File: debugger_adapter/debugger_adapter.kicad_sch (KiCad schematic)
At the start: 13 parts, among them X1 FT_CONN0_TAG, X10 FT_CONN_BREAKOUT, X11 DUT_CONN0_BREAKOUT, X12 VCC_SEL_UART, X13 DUT_CONN1_BREAKOUT, X2 FT_CONN1_TAG, X3 TAG_CONN_TAG, X4 FT_CONN_JTAG, X5 DUT_CONN_JTAG, X6 VCC_SEL_TAG, X7 VCC_SEL_JTAG, X8 FT_CONN_UART, X9 DUT_CONN_UART

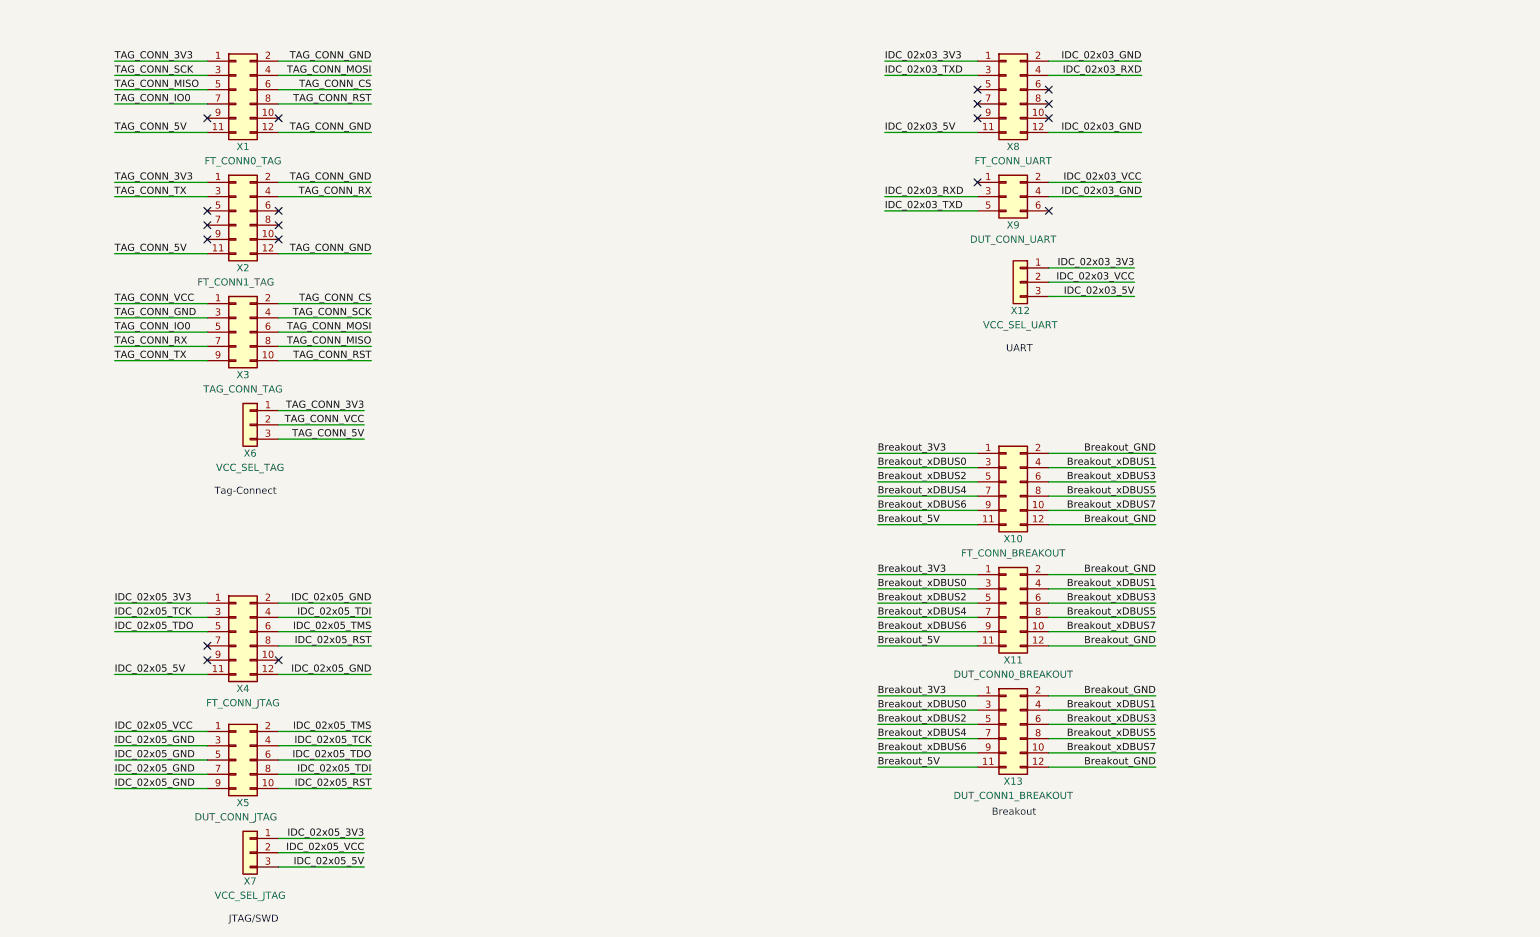
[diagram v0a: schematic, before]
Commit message: decrease clearance of copper pours
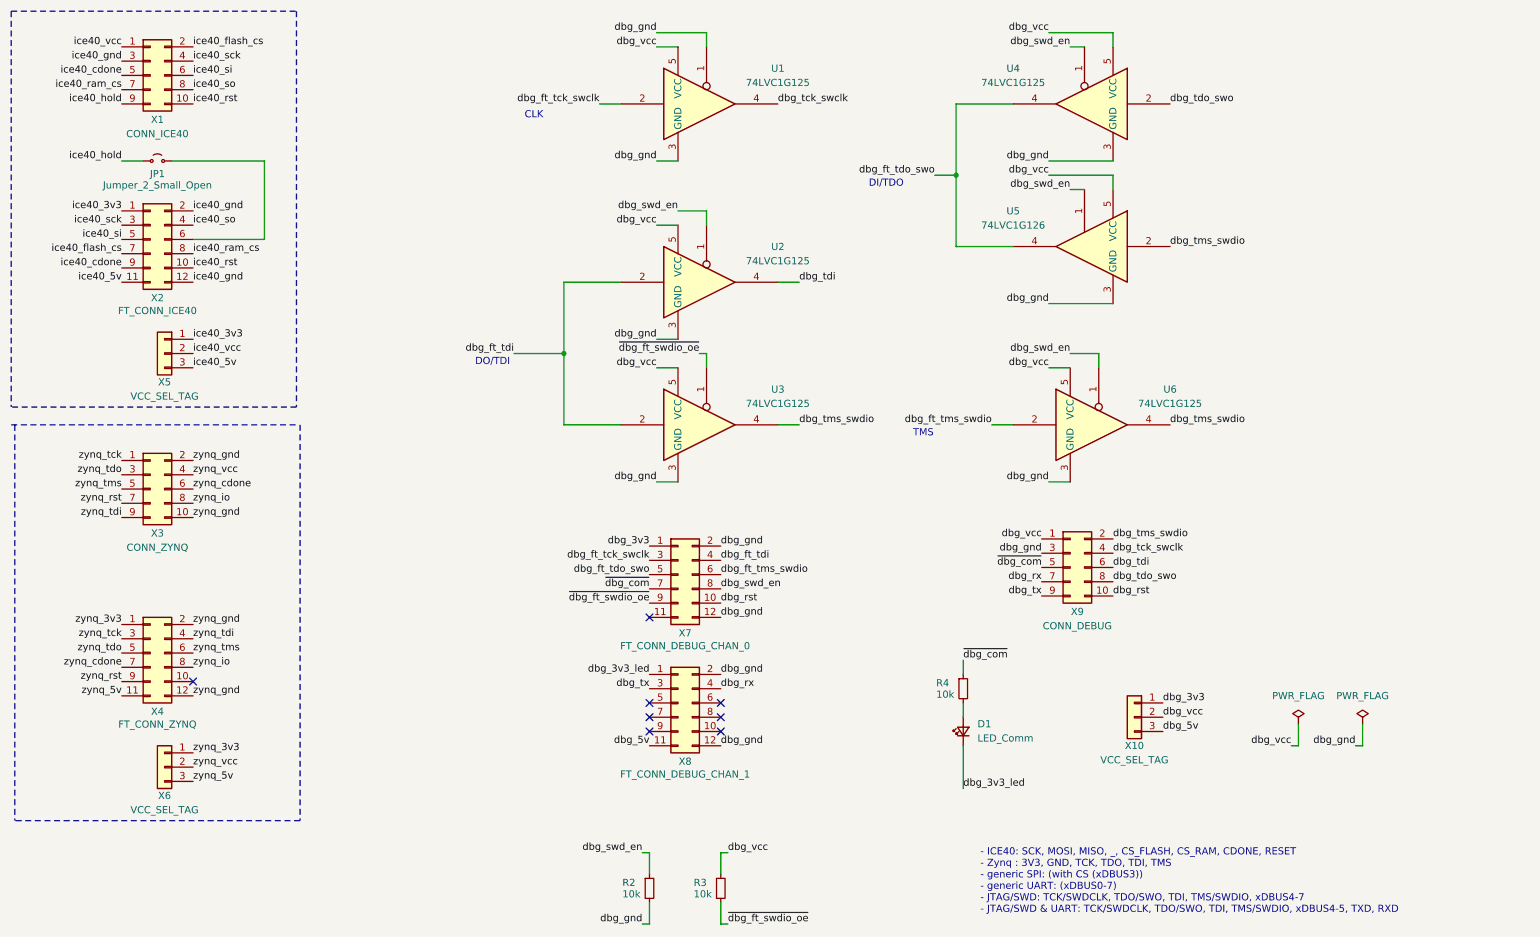
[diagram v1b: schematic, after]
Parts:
- removed X1: FT_CONN0_TAG, ft4232_debugger:header_male_02x06_HDRRA12W67P254_2X6_1524X254X503P, symbol Connector_Generic:Conn_02x06_Odd_Even
- removed X10: FT_CONN_BREAKOUT, ft4232_debugger:header_male_02x06_HDRRA12W67P254_2X6_1524X254X503P, symbol Connector_Generic:Conn_02x06_Odd_Even
- removed X11: DUT_CONN0_BREAKOUT, Connector_PinHeader_2.54mm:PinHeader_2x06_P2.54mm_Vertical_SMD, symbol Connector_Generic:Conn_02x06_Odd_Even
- removed X12: VCC_SEL_UART, Connector_PinHeader_2.54mm:PinHeader_1x03_P2.54mm_Vertical, symbol Connector_Generic:Conn_01x03
- removed X13: DUT_CONN1_BREAKOUT, Connector_PinHeader_2.54mm:PinHeader_2x06_P2.54mm_Vertical_SMD, symbol Connector_Generic:Conn_02x06_Odd_Even
- removed X5: DUT_CONN_JTAG, Connector_PinHeader_2.54mm:PinHeader_2x05_P2.54mm_Vertical_SMD, symbol Connector_Generic:Conn_02x05_Odd_Even
- removed X7: VCC_SEL_JTAG, Connector_PinHeader_2.54mm:PinHeader_1x03_P2.54mm_Vertical, symbol Connector_Generic:Conn_01x03
- removed X9: DUT_CONN_UART, ft4232_debugger:header_male_02x06_HDRRA12W67P254_2X6_1524X254X503P, symbol Connector_Generic:Conn_02x03_Odd_Even
- added D1: LED_Comm, LED_SMD:LED_0603_1608Metric, symbol Device:LED_Small
- added JP1: Jumper_2_Small_Open, Connector_PinHeader_2.54mm:PinHeader_1x02_P2.54mm_Vertical, symbol Jumper:Jumper_2_Small_Open
- added R2, R3, R4: 10k, Resistor_SMD:R_0402_1005Metric, symbol Device:R_Small
- added U1, U2, U3, U4, U6: 74LVC1G125, Package_TO_SOT_SMD:SOT-353_SC-70-5, symbol 74xGxx:74LVC1G125
- added U5: 74LVC1G126, Package_TO_SOT_SMD:SOT-353_SC-70-5, symbol 74xGxx:74LVC1G126
- added X1: CONN_ICE40, Connector_IDC:IDC-Header_2x05_P2.54mm_Vertical, symbol Connector_Generic:Conn_02x05_Odd_Even
- added X10, X5: VCC_SEL_TAG, Connector_PinHeader_2.54mm:PinHeader_1x03_P2.54mm_Vertical, symbol Connector_Generic:Conn_01x03
- added X7: FT_CONN_DEBUG_CHAN_0, ft4232_debugger:header_male_02x06_HDRRA12W67P254_2X6_1524X254X503P, symbol Connector_Generic:Conn_02x06_Odd_Even
- added X9: CONN_DEBUG, Connector_IDC:IDC-Header_2x05_P2.54mm_Vertical, symbol Connector_Generic:Conn_02x05_Odd_Even
- X2: value FT_CONN1_TAG -> FT_CONN_ICE40
- X3: value TAG_CONN_TAG -> CONN_ZYNQ; footprint Connector_PinHeader_2.54mm:PinHeader_2x05_P2.54mm_Vertical_SMD -> Connector_IDC:IDC-Header_2x05_P2.54mm_Vertical
- X4: value FT_CONN_JTAG -> FT_CONN_ZYNQ
- X8: value FT_CONN_UART -> FT_CONN_DEBUG_CHAN_1
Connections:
- net TAG_CONN_CS is gone; now on net zynq_gnd: X3.2 (Pin_2)
- net TAG_CONN_IO0 is gone; now on net zynq_tms: X3.5 (Pin_5)
- net TAG_CONN_MISO is gone; now on net zynq_io: X3.8 (Pin_8)
- net TAG_CONN_MOSI is gone; now on net zynq_cdone: X3.6 (Pin_6)
- net TAG_CONN_RST is gone; now on net zynq_gnd: X3.10 (Pin_10)
- net zynq_cdone: now reaches X4.7 (Pin_7)
- net zynq_rst: now reaches X4.9 (Pin_9)
- net zynq_rst: now also X3.7 (Pin_7)
- net ice40_rst: now reaches X2.10 (Pin_10)
- net ice40_rst: now also X1.10 (Pin_10)
- net ice40_si: now reaches X2.5 (Pin_5)
- net ice40_si: now also X1.6 (Pin_6)
- net at X2.6 (Pin_6): now also JP1.2 (B)
- net ice40_flash_cs: now reaches X2.7 (Pin_7)
- net ice40_flash_cs: now also X1.2 (Pin_2)
- net ice40_ram_cs: now reaches X2.8 (Pin_8)
- net ice40_ram_cs: now also X1.7 (Pin_7)
- net ice40_cdone: now reaches X2.9 (Pin_9)
- net ice40_cdone: now also X1.5 (Pin_5)
- net IDC_02x03_3V3 renamed dbg_3v3_led
- net dbg_3v3_led: now also D1.1 (K)
- net IDC_02x03_5V renamed dbg_5v
- net dbg_5v: now also X10.3 (Pin_3)
- net IDC_02x03_GND renamed dbg_gnd
- net dbg_gnd: now also R2.2, U1.1, U1.3 (GND), U2.3 (GND), U3.3 (GND), U4.3 (GND), U5.3 (GND), U6.3 (GND), X7.12 (Pin_12), X7.2 (Pin_2), X9.3 (Pin_3)
- net IDC_02x03_RXD renamed dbg_rx
- net dbg_rx: now also X9.7 (Pin_7)
- net IDC_02x03_TXD renamed dbg_tx
- net dbg_tx: now also X9.9 (Pin_9)
- net IDC_02x05_3V3 renamed zynq_3v3
- net zynq_3v3: now also X6.1 (Pin_1)
- net IDC_02x05_5V renamed zynq_5v
- net zynq_5v: now also X6.3 (Pin_3)
- net IDC_02x05_GND renamed zynq_gnd
- net IDC_02x05_RST renamed zynq_io
- net IDC_02x05_TCK renamed zynq_tck
- net zynq_tck: now also X3.1 (Pin_1)
- net IDC_02x05_TDI renamed zynq_tdi
- net zynq_tdi: now also X3.9 (Pin_9)
- net IDC_02x05_TDO renamed zynq_tdo
- net zynq_tdo: now also X3.3 (Pin_3)
- net IDC_02x05_TMS renamed zynq_tms
- net TAG_CONN_3V3 renamed ice40_3v3
- net ice40_3v3: now also X5.1 (Pin_1); no longer X6.1 (Pin_1)
- net TAG_CONN_5V renamed ice40_5v
- net ice40_5v: now also X5.3 (Pin_3); no longer X6.3 (Pin_3)
- net TAG_CONN_GND renamed ice40_gnd
- net ice40_gnd: now also X1.3 (Pin_3); no longer X3.3 (Pin_3)
- net TAG_CONN_RX renamed ice40_so
- net ice40_so: now also X1.8 (Pin_8); no longer X3.7 (Pin_7)
- net TAG_CONN_SCK renamed zynq_vcc
- net zynq_vcc: now also X6.2 (Pin_2)
- net TAG_CONN_TX renamed ice40_sck
- net ice40_sck: now also X1.4 (Pin_4); no longer X3.9 (Pin_9)
- removed net TAG_CONN_VCC: X3.1 (Pin_1), X6.2 (Pin_2)
- new net: D1.2 (A), R4.2
- new net dbg_3v3: X10.1 (Pin_1), X7.1 (Pin_1)
- new net dbg_ft_tck_swclk: U1.2, X7.3 (Pin_3)
- new net dbg_ft_tdi: U2.2, U3.2, X7.4 (Pin_4)
- new net dbg_ft_tdo_swo: U4.4, U5.4, X7.5 (Pin_5)
- new net dbg_ft_tms_swdio: U6.2, X7.6 (Pin_6)
- new net dbg_rst: X7.10 (Pin_10), X9.10 (Pin_10)
- new net dbg_swd_en: R2.1, U2.1, U4.1, U5.1, U6.1, X7.8 (Pin_8)
- new net dbg_tck_swclk: U1.4, X9.4 (Pin_4)
- new net dbg_tdi: U2.4, X9.6 (Pin_6)
- new net dbg_tdo_swo: U4.2, X9.8 (Pin_8)
- new net dbg_tms_swdio: U3.4, U5.2, U6.4, X9.2 (Pin_2)
- new net dbg_vcc: R3.1, U1.5 (VCC), U2.5 (VCC), U3.5 (VCC), U4.5 (VCC), U5.5 (VCC), U6.5 (VCC), X10.2 (Pin_2), X9.1 (Pin_1)
- new net ice40_hold: JP1.1 (A), X1.9 (Pin_9)
- new net ice40_vcc: X1.1 (Pin_1), X5.2 (Pin_2)
- new net ~{dbg_com}: R4.1, X7.7 (Pin_7), X9.5 (Pin_5)
- new net ~{dbg_ft_swdio_oe}: R3.2, U3.1, X7.9 (Pin_9)
- no-connect marks 19 -> 8
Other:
- note added: "- ICE40: SCK, MOSI, MISO, _, CS_FLASH, CS_RAM, CDONE, RESET - Zynq : 3V3, GND, TCK, TDO, TDI, TMS - generic SPI: (with CS (xDBUS3)) - generic UART: (xDBUS0-7) - JTAG/SWD: TCK/SWDCLK, TDO/SWO, TDI, TMS/SWDIO, xDBUS4-7 - JTAG/SWD & UART: TCK/SWDCLK, TDO/SWO, TDI, TMS/SWDIO, xDBUS4-5, TXD, RXD"
- note added: "CLK"
- note added: "DI/TDO"
- note added: "DO/TDI"
- note added: "TMS"
- note removed: "Breakout"
- note removed: "JTAG/SWD"
- note removed: "Tag-Connect"
- note removed: "UART"
- title: (none) -> FT4232 Debugger Adapter
